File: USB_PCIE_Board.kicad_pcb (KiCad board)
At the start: 2 copper layers, 98.2 x 111.5 mm, 171 parts, among them J1 Bus_PCI_Express_x1, J2 GSB4116341HR, J3 GSB4116341HR, J4 GSB4116341HR, J5 GSB4116341HR, Q1 2SA1576AT106R, Q2 2SC4081T106R, Q4 DMT6016LSS-13, Q5 SI4134DY-T1-GE3, U1 UPD720201K8-711-BAC-A, U10 AP2191SG-13, U11 AP2191SG-13, U12 SP3011-06UTG, U13 SP3011-06UTG, U14 SP3011-06UTG, U15 SP3011-06UTG, U2 MX25L4006EM1I-12G, U3 LM22678TJ-5.0/NOPB, U4 LTC3872ETS8-TRPBF, U5 RT5762CHGH6F, U6 641737-1, U7 AP7215-33YG-13, U8 AP2191SG-13, U9 AP2191SG-13, X1 CS14522-24M

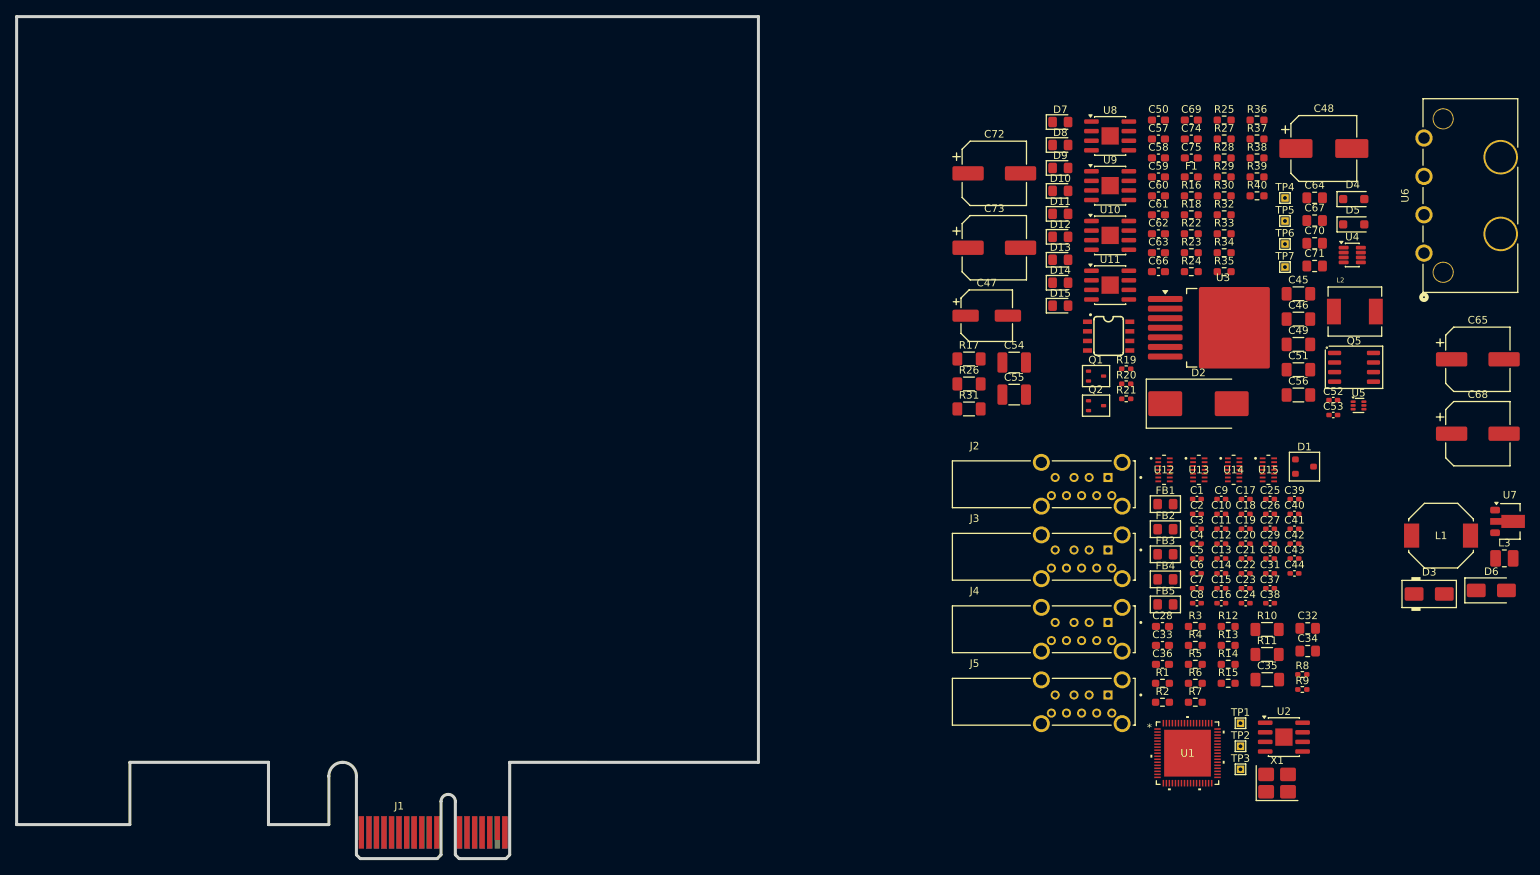
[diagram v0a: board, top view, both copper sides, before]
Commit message: Place all components except host chip decoupling caps and the crystal circuit.
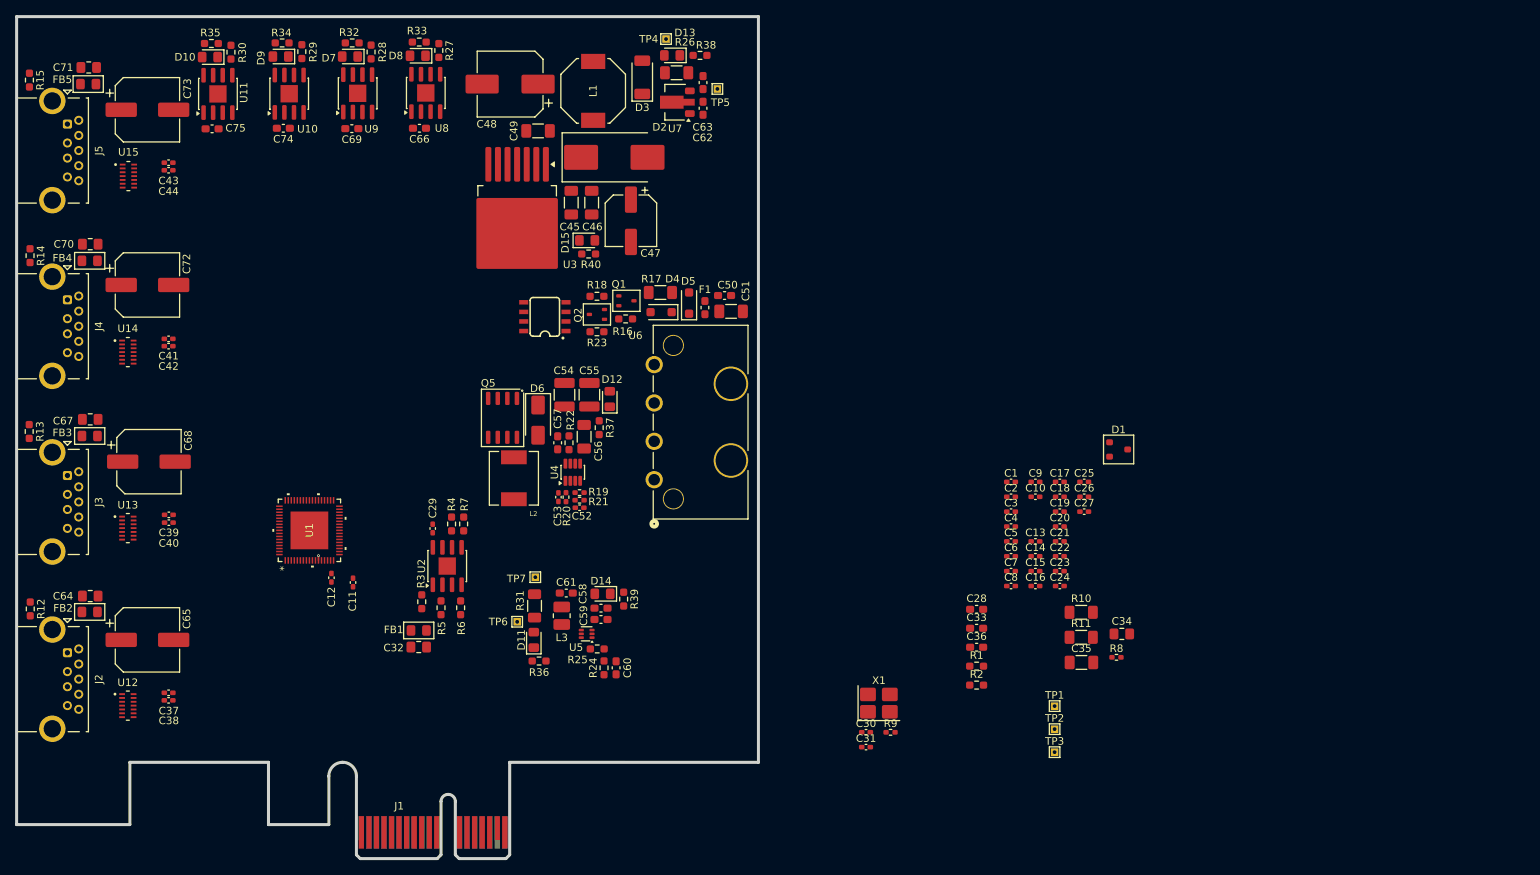
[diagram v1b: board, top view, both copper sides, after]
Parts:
- D3: value RB081L-20 -> RSX501LAM20TR; footprint PCM_Diode_SMD_AKL:D_SMA -> Diode_SMD:D_SOD-128
- J2, J3, J4, J5: value GSB4116341HR -> 0484050001; footprint 0_Custom:AMPHENOL_GSB4116341HR -> 0_Custom:USB3_A_Molex_48406-0001_Horizontal_Stacked
- Q5: footprint PCM_Package_SO_AKL:SO-8_3.9x4.9mm_P1.27mm -> 0_Custom:SO-8_3.9x4.9mm_P1.27mm
- TP4, TP5, TP6, TP7: value D0.5mm -> TestPoint
- U1: footprint 0_Custom:QFN68_8X8_REN-M -> 0_Custom:QFN68_8X8_REN-M_Hand_Soldering
- U10, U11, U2, U8, U9: footprint Package_SO:HSOP-8-1EP_3.9x4.9mm_P1.27mm_EP2.3x2.3mm -> 0_Custom:HSOP-8-1EP_3.9x4.9mm_P1.27mm_EP2.3x2.3mm
- moved C65 180.1 mm to (68.8, 120.8)
- moved R15 177.7 mm to (53.1, 46.7), turned to -90 degrees
- moved C68 176.0 mm to (69.0, 97.2)
- moved C64 170.5 mm to (61.2, 115.0), turned to 180 degrees
- moved R14 167.6 mm to (53.2, 69.9), turned to -90 degrees
- moved C71 164.5 mm to (61.0, 45.0), turned to 180 degrees
- moved C67 164.3 mm to (61.2, 91.6), turned to 180 degrees
- moved C70 162.1 mm to (61.2, 68.4), turned to 180 degrees
- moved R13 161.3 mm to (53.1, 93.2), turned to -90 degrees
- moved R12 158.6 mm to (53.3, 116.7), turned to -90 degrees
- moved FB5 158.4 mm to (60.9, 47.2), turned to 180 degrees
- moved C44 158.4 mm to (71.6, 58.6)
- moved C43 158.0 mm to (71.6, 57.6), turned to 180 degrees
- moved U15 155.9 mm to (66.3, 59.4)
- moved J5 154.6 mm to (58.2, 52.5), turned to -90 degrees
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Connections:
- net PETXN_H renamed PETX_HN
- net PETXP_H renamed PETX_HP
- net U3TXDN1_H renamed U3TXD1_HN
- net U3TXDN2_H renamed U3TXD2_HN
- net U3TXDN3_H renamed U3TXD3_HN
- net U3TXDN4_H renamed U3TXD4_HN
- net U3TXDP1_H renamed U3TXD1_HP
- net U3TXDP2_H renamed U3TXD2_HP
- net U3TXDP3_H renamed U3TXD3_HP
- net U3TXDP4_H renamed U3TXD4_HP
- C37 pad 2: U3TXDP4 -> U3TXD4P
- C38 pad 1: U3TXDN4 -> U3TXD4N
- C39 pad 2: U3TXDP3 -> U3TXD3P
- C40 pad 1: U3TXDN3 -> U3TXD3N
- C41 pad 2: U3TXDP2 -> U3TXD2P
- C42 pad 1: U3TXDN2 -> U3TXD2N
- C43 pad 2: U3TXDP1 -> U3TXD1P
- C44 pad 1: U3TXDN1 -> U3TXD1N
- J2 pad 2: U2DM4 -> U2D4N
- J2 pad 3: U2DP4 -> U2D4P
- J2 pad 5: U3RXDN4 -> U3RXD4N
- J2 pad 6: U3RXDP4 -> U3RXD4P
- J2 pad 8: U3TXDN4 -> U3TXD4N
- J2 pad 9: U3TXDP4 -> U3TXD4P
- J3 pad 2: U2DM3 -> U2D3N
- J3 pad 3: U2DP3 -> U2D3P
- J3 pad 5: U3RXDN3 -> U3RXD3N
- J3 pad 6: U3RXDP3 -> U3RXD3P
- J3 pad 8: U3TXDN3 -> U3TXD3N
- J3 pad 9: U3TXDP3 -> U3TXD3P
- J4 pad 2: U2DM2 -> U2D2N
- J4 pad 3: U2DP2 -> U2D2P
- J4 pad 5: U3RXDN2 -> U3RXD2N
- J4 pad 6: U3RXDP2 -> U3RXD2P
- J4 pad 8: U3TXDN2 -> U3TXD2N
- J4 pad 9: U3TXDP2 -> U3TXD2P
- J5 pad 2: U2DM1 -> U2D1N
- J5 pad 3: U2DP1 -> U2D1P
- J5 pad 5: U3RXDN1 -> U3RXD1N
- J5 pad 6: U3RXDP1 -> U3RXD1P
- J5 pad 8: U3TXDN1 -> U3TXD1N
- J5 pad 9: U3TXDP1 -> U3TXD1P
- U1 pad 38: U3RXDP1 -> U3RXD1P
- U1 pad 39: U3RXDN1 -> U3RXD1N
- U1 pad 41: U2DP1 -> U2D1P
- U1 pad 42: U2DM1 -> U2D1N
- U1 pad 47: U3RXDP2 -> U3RXD2P
- U1 pad 48: U3RXDN2 -> U3RXD2N
- U1 pad 50: U2DP2 -> U2D2P
- U1 pad 51: U2DM2 -> U2D2N
- U1 pad 55: U3RXDP3 -> U3RXD3P
- U1 pad 56: U3RXDN3 -> U3RXD3N
- U1 pad 58: U2DP3 -> U2D3P
- U1 pad 59: U2DM3 -> U2D3N
- U1 pad 64: U3RXDP4 -> U3RXD4P
- U1 pad 65: U3RXDN4 -> U3RXD4N
- U1 pad 67: U2DP4 -> U2D4P
- U1 pad 68: U2DM4 -> U2D4N
- U12 pad 1: U3TXDN4 -> U3TXD4P
- U12 pad 11: U3RXDP4 -> U3RXD4N
- U12 pad 12: U3RXDN4 -> U3RXD4P
- U12 pad 13: U3TXDP4 -> U3TXD4N
- U12 pad 14: U3TXDN4 -> U3TXD4P
- U12 pad 2: U3TXDP4 -> U3TXD4N
- U12 pad 3: U3RXDN4 -> U3RXD4P
- U12 pad 4: U3RXDP4 -> U3RXD4N
- U12 pad 6: U2DM4 -> U2D4P
- U12 pad 7: U2DP4 -> U2D4N
- U12 pad 8: U2DP4 -> U2D4N
- U12 pad 9: U2DM4 -> U2D4P
- U13 pad 1: U3TXDN3 -> U3TXD3P
- U13 pad 11: U3RXDP3 -> U3RXD3N
- U13 pad 12: U3RXDN3 -> U3RXD3P
- U13 pad 13: U3TXDP3 -> U3TXD3N
- U13 pad 14: U3TXDN3 -> U3TXD3P
- U13 pad 2: U3TXDP3 -> U3TXD3N
- U13 pad 3: U3RXDN3 -> U3RXD3P
- U13 pad 4: U3RXDP3 -> U3RXD3N
- U13 pad 6: U2DM3 -> U2D3P
- U13 pad 7: U2DP3 -> U2D3N
- U13 pad 8: U2DP3 -> U2D3N
- U13 pad 9: U2DM3 -> U2D3P
- U14 pad 1: U3TXDN2 -> U3TXD2P
- U14 pad 11: U3RXDP2 -> U3RXD2N
- U14 pad 12: U3RXDN2 -> U3RXD2P
- U14 pad 13: U3TXDP2 -> U3TXD2N
- U14 pad 14: U3TXDN2 -> U3TXD2P
- U14 pad 2: U3TXDP2 -> U3TXD2N
- U14 pad 3: U3RXDN2 -> U3RXD2P
- U14 pad 4: U3RXDP2 -> U3RXD2N
- U14 pad 6: U2DM2 -> U2D2P
- U14 pad 7: U2DP2 -> U2D2N
- U14 pad 8: U2DP2 -> U2D2N
- U14 pad 9: U2DM2 -> U2D2P
- U15 pad 1: U3TXDN1 -> U3TXD1P
- U15 pad 11: U3RXDP1 -> U3RXD1N
- U15 pad 12: U3RXDN1 -> U3RXD1P
- U15 pad 13: U3TXDP1 -> U3TXD1N
- U15 pad 14: U3TXDN1 -> U3TXD1P
- U15 pad 2: U3TXDP1 -> U3TXD1N
- U15 pad 3: U3RXDN1 -> U3RXD1P
- U15 pad 4: U3RXDP1 -> U3RXD1N
- U15 pad 6: U2DM1 -> U2D1P
- U15 pad 7: U2DP1 -> U2D1N
- U15 pad 8: U2DP1 -> U2D1N
- U15 pad 9: U2DM1 -> U2D1P
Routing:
- net +1V05: track 0.00 -> 0.63 mm, vias 0 -> 1
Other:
- copper layers 2 -> 4

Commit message: Placed all parts on PCB
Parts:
- C1, C10, C11, C12, C13, C14, C15, C17, C18, C19, C2, C20, C21, C22, C23, C25, C3, C4, C5, C6, C7, C8, C9: moved to B.Cu
- moved TP2 107.5 mm to (83.0, 114.3)
- moved C26 104.8 mm to (89.2, 117.3), turned to 90 degrees
- moved R8 104.8 mm to (94.8, 100.4), turned to -90 degrees
- moved C25 104.2 mm to (89.2, 111.0), turned to -90 degrees
- moved C22 104.2 mm to (85.6, 103.4), turned to 180 degrees
- moved C27 103.6 mm to (90.1, 117.3), turned to 90 degrees
- moved C19 102.5 mm to (87.2, 101.7), turned to 90 degrees
- moved C17 102.0 mm to (88.2, 111.0), turned to 90 degrees
- moved D1 101.6 mm to (97.5, 114.3), turned to 90 degrees
- moved C15 101.1 mm to (85.6, 104.4)
- moved C14 100.8 mm to (85.6, 107.4)
- moved C35 99.5 mm to (93.4, 132.8), turned to 180 degrees
- moved C1 98.0 mm to (85.6, 109.4)
- moved C8 97.8 mm to (85.6, 106.4)
- moved C3 97.7 mm to (85.6, 108.4)
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
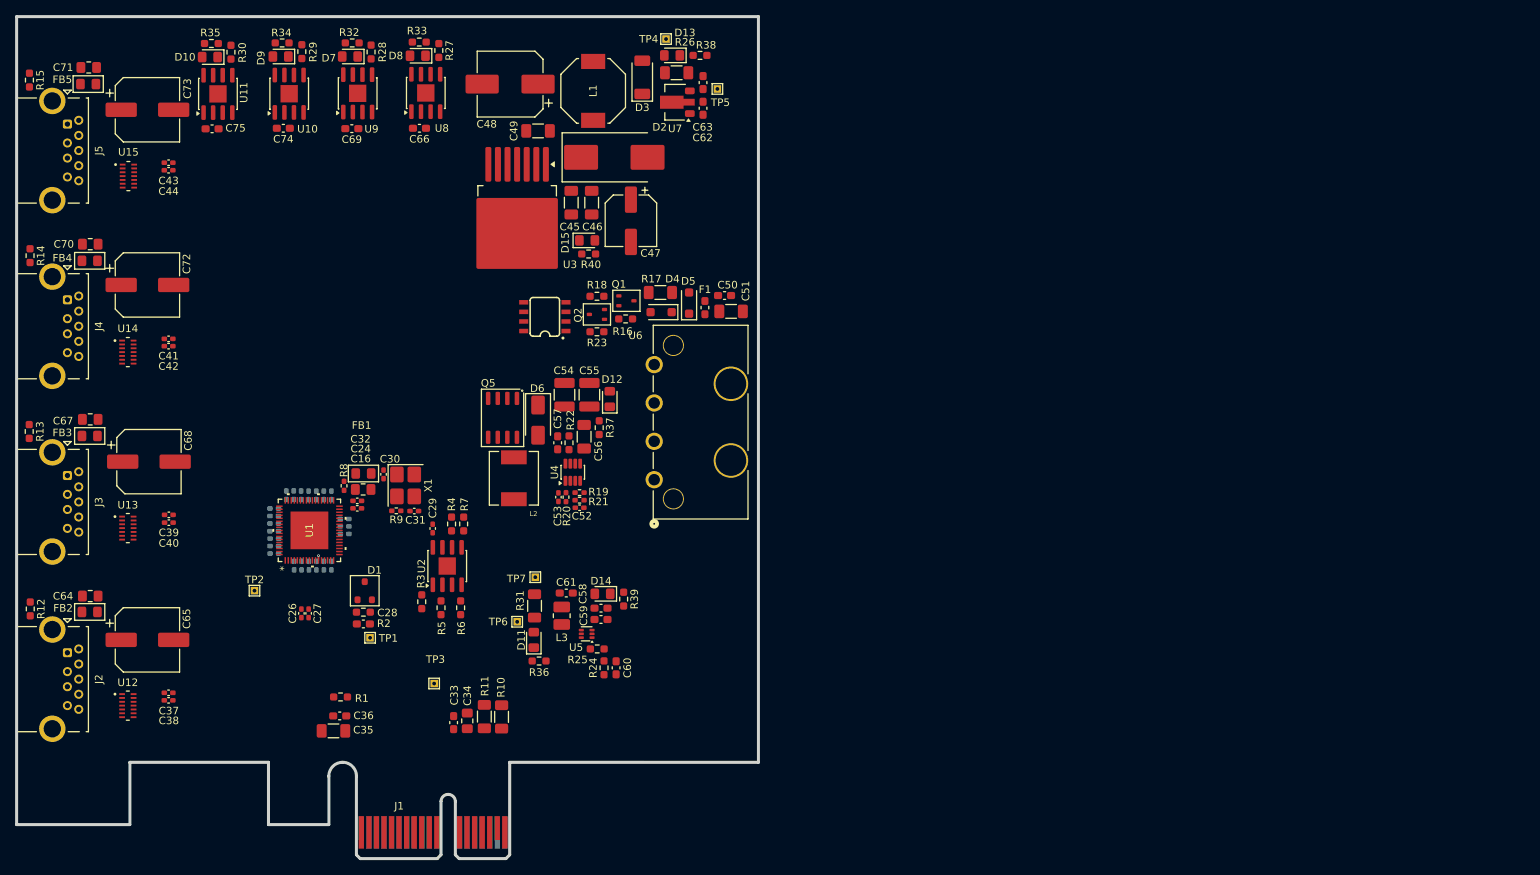
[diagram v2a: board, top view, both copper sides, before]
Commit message: Complete first pass of routing all nets without DRC
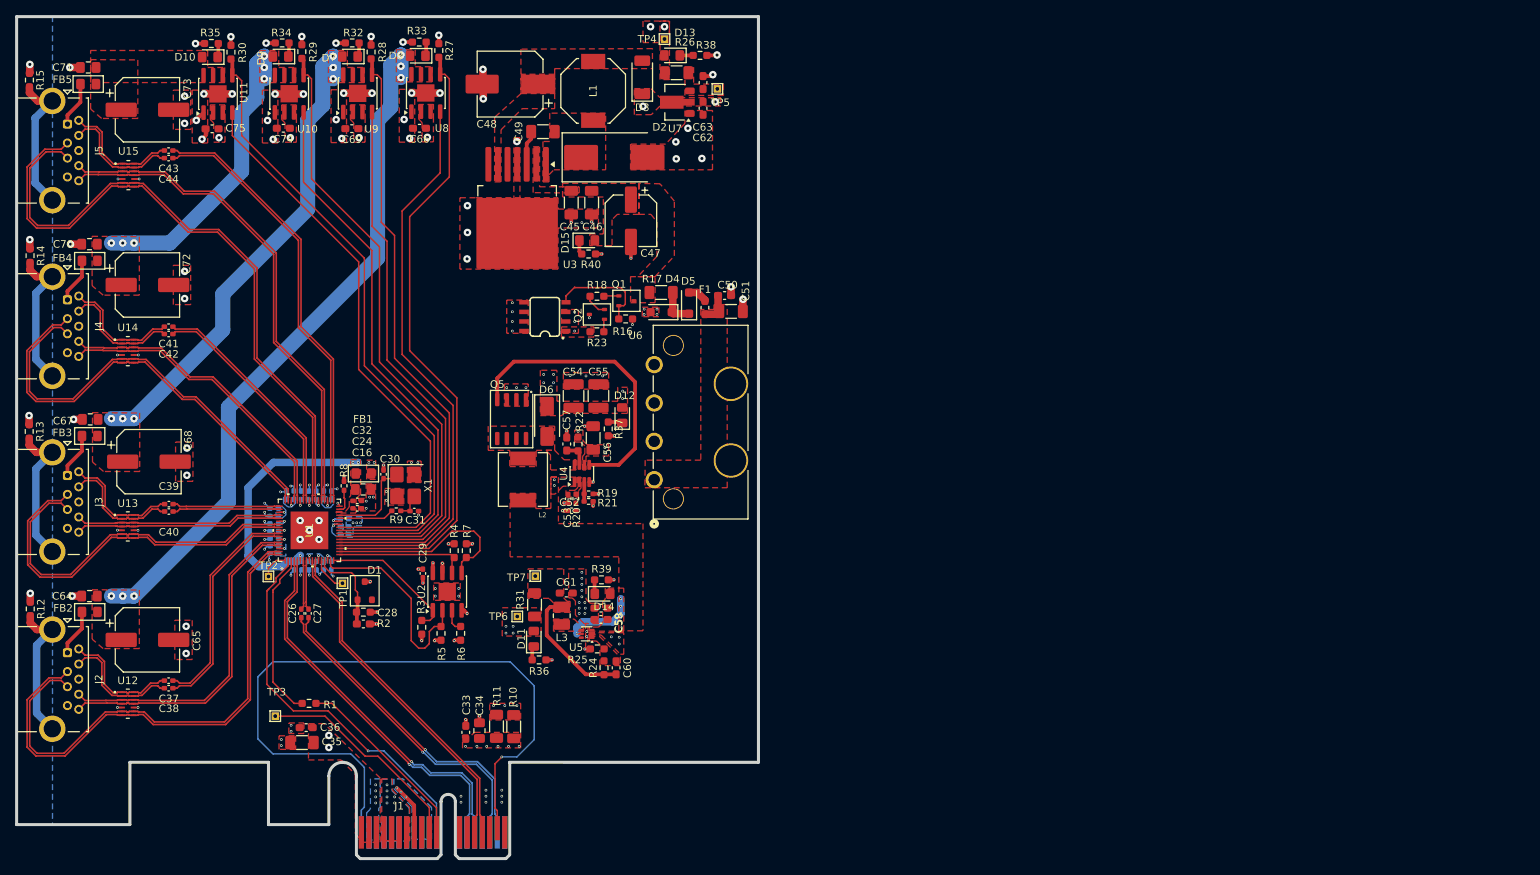
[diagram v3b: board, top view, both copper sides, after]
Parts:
- U2: footprint 0_Custom:HSOP-8-1EP_3.9x4.9mm_P1.27mm_EP2.3x2.3mm -> 0_Custom:HSOP-8-1EP_3.9x4.9mm_P1.27mm_EP2.3x2.3mm_FLASH
- moved TP3 21.5 mm to (85.7, 130.9)
- moved TP1 8.09 mm to (94.6, 113.3)
- moved C29 6.09 mm to (105.2, 112.0)
- moved C36 4.70 mm to (89.8, 132.4)
- moved C35 4.45 mm to (89.2, 134.4)
- moved R1 4.26 mm to (90.2, 129.2)
- moved R39 3.89 mm to (128.9, 112.8), turned to 0 degrees
- moved R4 3.55 mm to (109.4, 109.0)
- moved R7 3.55 mm to (111.0, 109.0)
- moved R3 3.39 mm to (105.1, 119.1)
- moved R5 3.39 mm to (107.7, 119.9)
- moved R6 3.39 mm to (110.2, 119.9)
- moved U2 3.39 mm to (108.5, 114.4)
- moved D12 2.71 mm to (131.7, 91.0)
- moved TP2 2.64 mm to (84.8, 112.4)
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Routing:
- net PRSNT: track 0.00 -> 93.1 mm, vias 0 -> 1
- net VCCCH4: track 0.00 -> 92.3 mm, vias 0 -> 6
- net GND: track 0.00 -> 86.0 mm, vias 0 -> 164
- net OCI1B: track 0.00 -> 85.1 mm
- net U2D1N: track 0.00 -> 84.9 mm
- net U2D1P: track 0.00 -> 84.4 mm
- net OCI4B: track 0.00 -> 84.1 mm
- net OCI2B: track 0.00 -> 83.2 mm
- net OCI3B: track 0.00 -> 81.4 mm
- net Earth: track 0.00 -> 76.9 mm
- net PPON1: track 0.00 -> 76.7 mm
- net PPON4: track 0.00 -> 75.3 mm
- net PPON2: track 0.00 -> 74.7 mm
- net PPON3: track 0.00 -> 72.9 mm
- net U2D4N: track 0.00 -> 69.2 mm
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- added copper zone on B.Cu, net +12V
- added copper zone on F.Cu, net +12V
- added copper zone on In2.Cu, net +12V
- added copper zone on F.Cu, net +12V_IN
- added copper zone on B.Cu, net +1V05
- added copper zone on F.Cu, net +1V05
- added copper zone on In2.Cu, net +1V05
- added copper zone on F.Cu, net +3V3
- added copper zone on In2.Cu, net +3V3
- added copper zone on F.Cu, net +3V3A
- added copper zone on B.Cu, net +3V3_DUAL
- added copper zone on F.Cu, net +3V3_DUAL
- added copper zone on In2.Cu, net +3V3_DUAL
- added copper zone on B.Cu, net +3V3_INT
- added copper zone on F.Cu, net +3V3_INT
- added copper zone on F.Cu, net +3V3_SW
- added copper zone on In2.Cu, net +3V3_SW
- added copper zone on F.Cu, net +5V
- added copper zone on In2.Cu, net +5V
- added copper zone on B.Cu, net Earth
- added copper zone on B.Cu, net GND
- added copper zone on F.Cu, net GND
- added copper zone on In1.Cu, net GND
- added copper zone on F.Cu, net Net-(C60-Pad1)
- added copper zone on F.Cu, net Net-(D2-K)
- added copper zone on F.Cu, net Net-(D3-A)
- added copper zone on F.Cu, net Net-(D6-A)
- added copper zone on F.Cu, net Net-(U4-ITH)
- added copper zone on F.Cu, net Net-(U5-FB)
- added copper zone on F.Cu, net Net-(U5-SW)
- added copper zone on F.Cu, net Net-(U6-+12V)
- added copper zone on F.Cu, net Net-(U7-VO)
- added copper zone on F.Cu, net VCCCH1
- added copper zone on F.Cu, net VCCCH2
- added copper zone on F.Cu, net VCCCH3
- added copper zone on F.Cu, net VCCCH4
